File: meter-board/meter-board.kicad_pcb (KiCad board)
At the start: 4 copper layers, 100 x 50 mm, 291 parts, among them J1 2-1445053-2, J2 3-794636-8, J3 2-1445053-4, Q1 PMN100EPAX, Q2 2N7002K-AU_R1_000A2, U1 AP66300QFVBW-13, U10 TLV1814RTER, U11 TLV1814RTER, U12 TLV1814RTER, U13 TLV1814RTER, U14 TLV1814RTER, U15 TLV1814RTER, U16 TBD62183AFNG,EL, U17 TBD62183AFNG,EL, U18 TBD62183AFNG,EL, U19 TBD62183AFNG,EL, U2 TS431BIYLT, U20 TLV1814RTER, U21 SN74HC595BRWNR, U22 SN74HC595BRWNR, U23 SN74HC595BRWNR, U24 TBD62783AFNG,EL, U25 TBD62183AFNG,EL, U26 TBD62183AFNG,EL, U27 SN74LV4T125RGYR, U3 ACSC02-41SURKWA-F01, U4 ACSC02-41SURKWA-F01, U5 ACSC02-41SURKWA-F01, U6 157121S12700, U7 157121S12700, U8 157121S12700, U9 TLV1814RTER

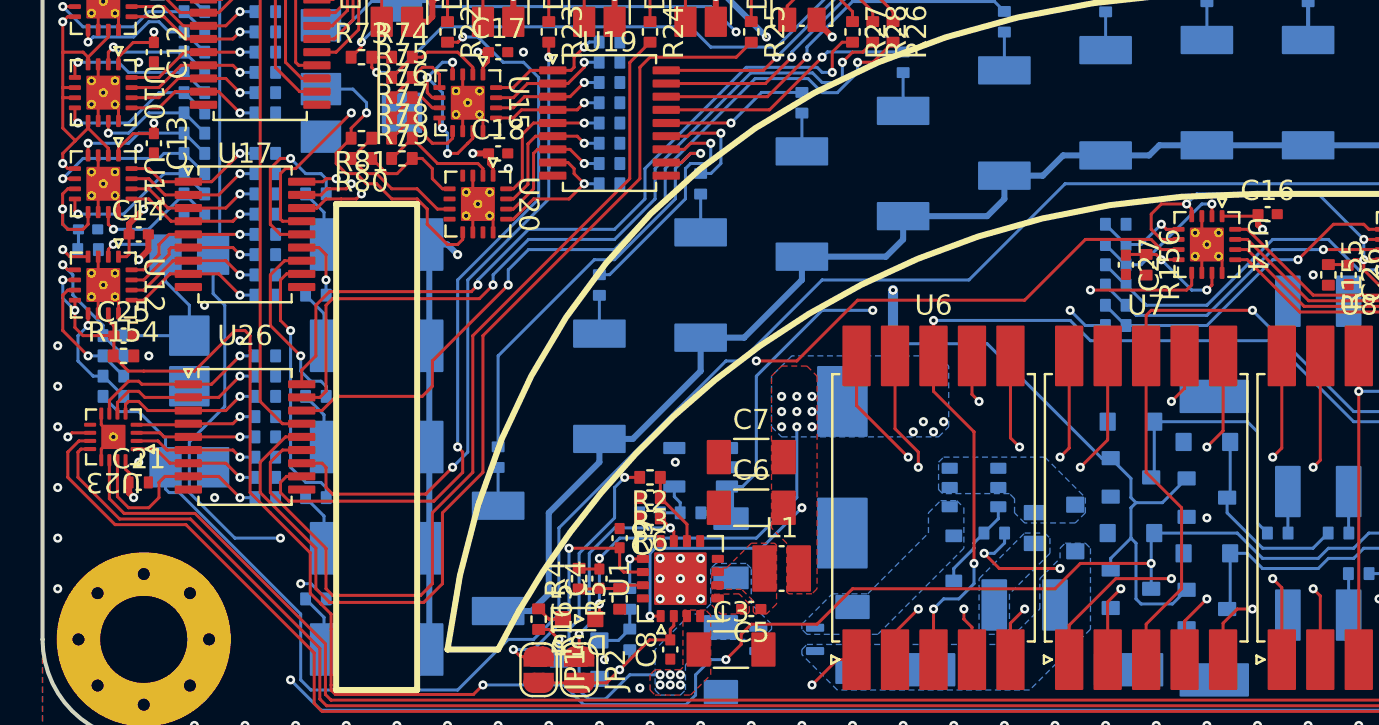
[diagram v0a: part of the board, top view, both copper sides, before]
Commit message: update patterns
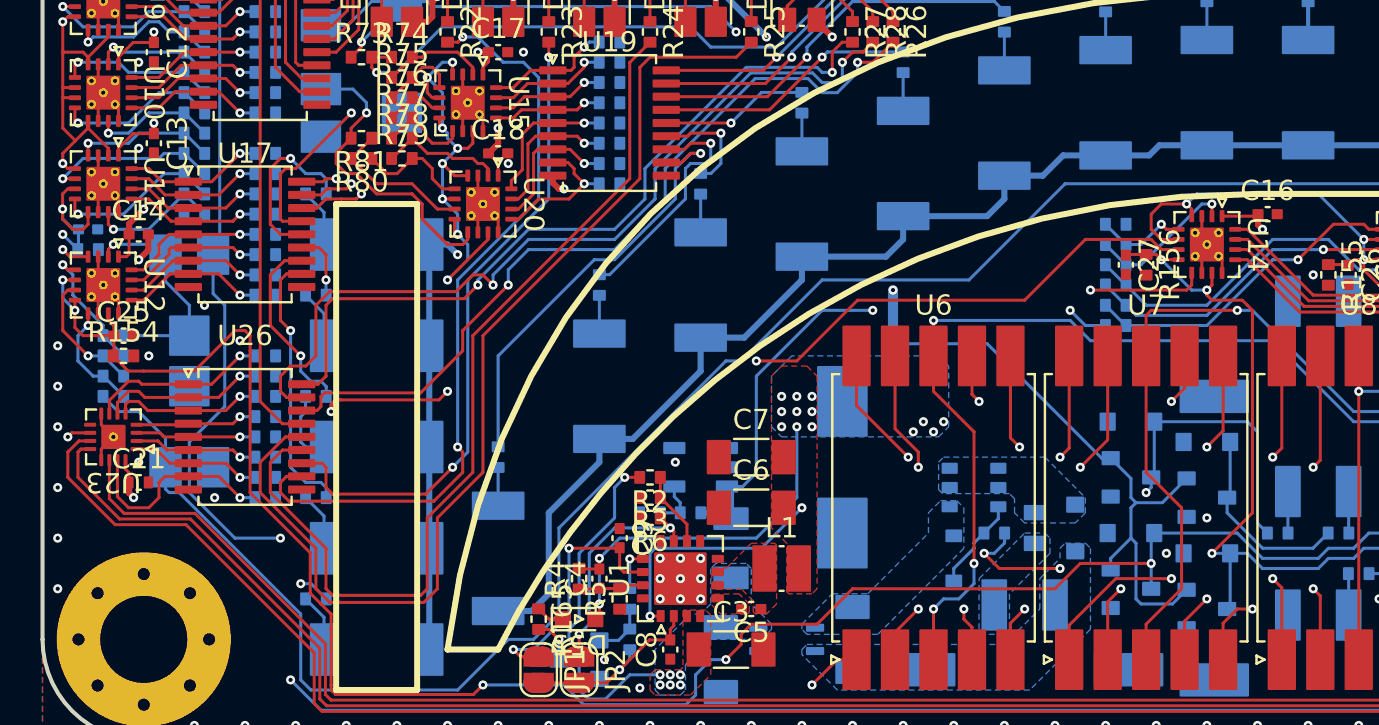
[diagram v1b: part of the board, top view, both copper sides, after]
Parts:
- moved U20 0.25 mm to (21.8, 23.5)
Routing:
- net /G6R6_AIN: track 45.2 -> 120.0 mm, vias 4 -> 8
- net /R10_AIN: track 31.5 -> 61.4 mm, vias 6 -> 11
- net /RGB_G: track 40.0 -> 41.9 mm
- net GND: track 50.8 -> 52.2 mm, vias 126 -> 128
- net +5VA: track 181.5 -> 182.7 mm
- net Net-(D11-K): track 2.88 -> 3.60 mm

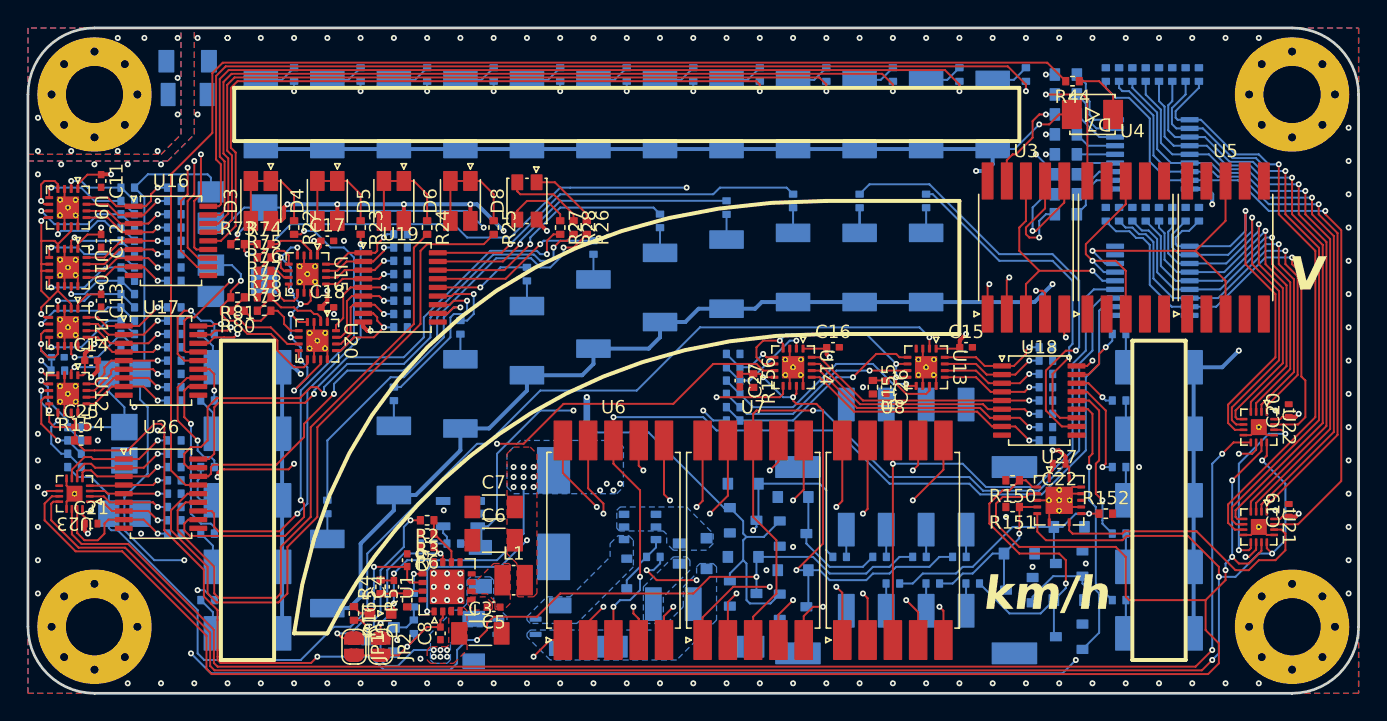
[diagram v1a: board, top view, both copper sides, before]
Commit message: update patterns
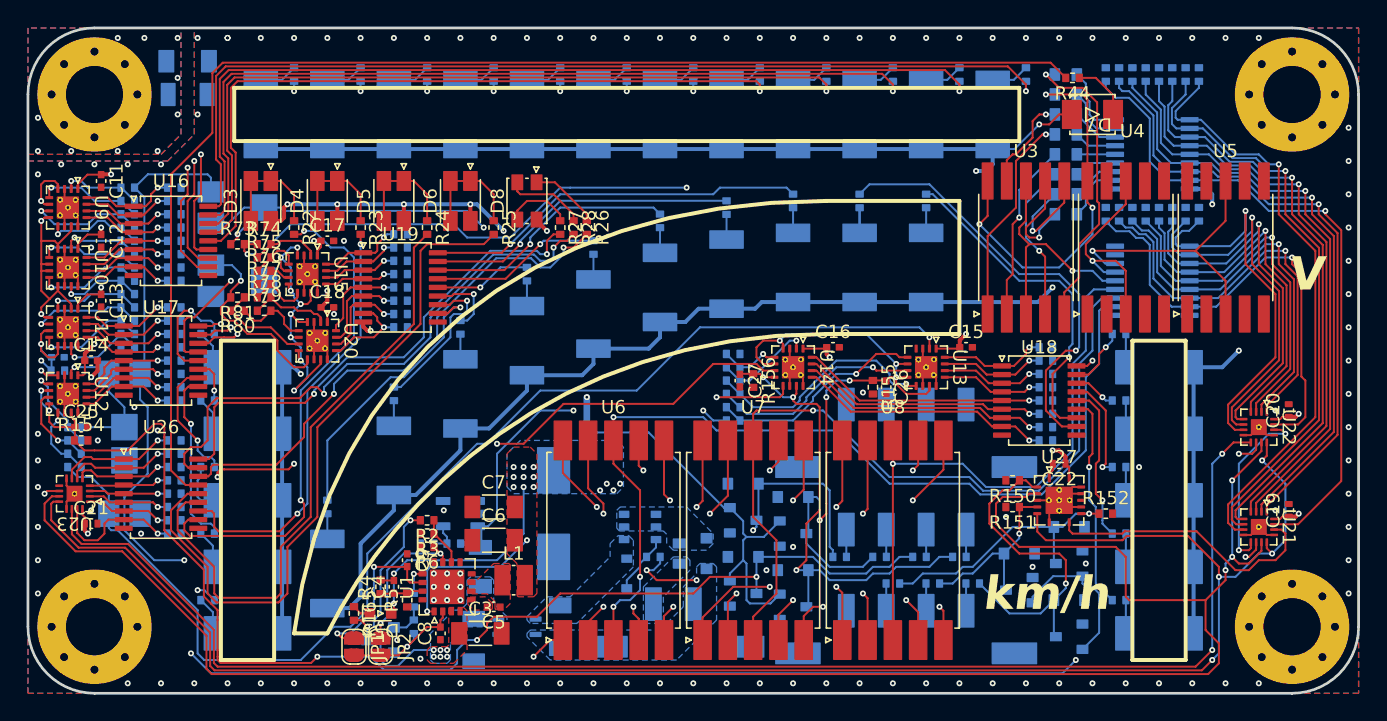
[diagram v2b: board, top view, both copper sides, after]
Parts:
- moved R44 0.25 mm to (78.5, 3.75)
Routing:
- net /7seg_G: track 44.5 -> 93.1 mm, vias 4 -> 6
- net /G5_AIN: track 32.8 -> 49.0 mm, vias 3 -> 6
- net /7seg_C: track 50.4 -> 42.3 mm, vias 5 -> 4
- net /7seg_E: track 57.0 -> 55.7 mm, vias 5 -> 4
- net /7seg_CC4: track 17.3 -> 18.2 mm
- net Net-(U13D--): track 17.1 -> 17.8 mm
- net /R10_R9: track 33.8 -> 33.2 mm
- net /R10_R10: track 26.1 -> 25.5 mm
- net /7seg_DP: track 51.8 -> 51.4 mm, vias 5 -> 4
- net /7seg_D: track 44.2 -> 43.8 mm, vias 5 -> 4

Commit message: update patterns
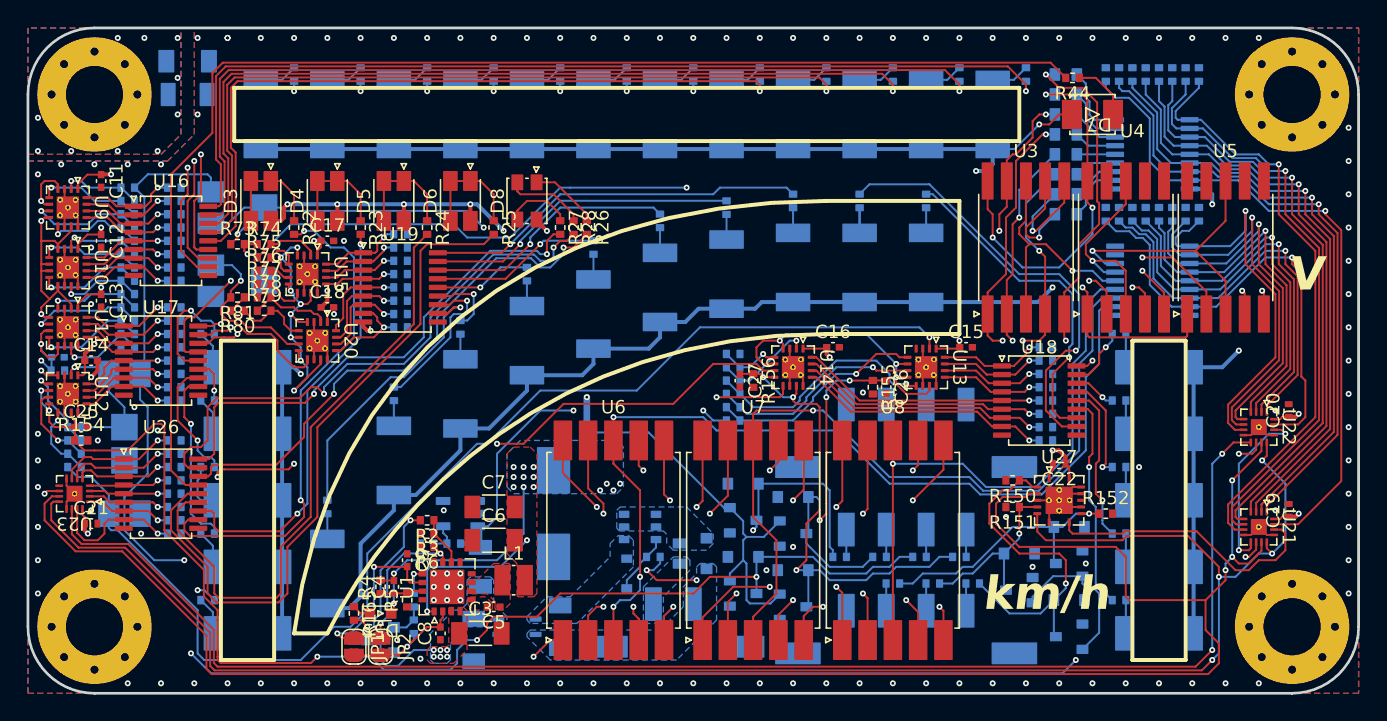
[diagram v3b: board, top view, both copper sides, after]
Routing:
- net /7seg_DP: track 51.4 -> 103.6 mm, vias 4 -> 7
- net /7seg_C: track 42.3 -> 93.8 mm, vias 4 -> 7
- net /7seg_D: track 43.8 -> 93.6 mm, vias 4 -> 7
- net /7seg_E: track 55.7 -> 104.1 mm, vias 4 -> 6
- net /7seg_F: track 44.5 -> 76.9 mm, vias 4 -> 5
- net /7seg_A: track 35.5 -> 63.2 mm
- net /7seg_B: track 41.5 -> 68.6 mm
- net +5VA: track 182.7 -> 181.3 mm
- net /7seg_G: track 93.1 -> 91.8 mm

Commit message: finish wiring
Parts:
- moved R156 1.25 mm to (53.2, 26.5)
- moved C27 0.75 mm to (54.2, 26.5)
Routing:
- net /R5_AIN: track 98.9 -> 193.3 mm, vias 6 -> 9
- net /R10_AIN: track 61.1 -> 121.6 mm, vias 11 -> 12
- net /7seg_B: track 68.6 -> 97.3 mm, vias 4 -> 7
- net /7seg_F: track 76.9 -> 101.8 mm, vias 5 -> 6
- net /7seg_A: track 63.2 -> 87.4 mm, vias 4 -> 6
- net /7seg_G: track 91.8 -> 105.6 mm, vias 6 -> 7
- net +5VD: track 333.2 -> 343.9 mm, vias 36 -> 37
- net +5VA: track 181.3 -> 182.2 mm
- net GND: vias 128 -> 132
